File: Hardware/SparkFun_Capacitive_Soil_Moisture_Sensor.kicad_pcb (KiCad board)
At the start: 2 copper layers, 15.2 x 73.4 mm, 53 parts, among them J1 Qwiic_RA, J2 Qwiic_RA, U1 CY8CMBR3102

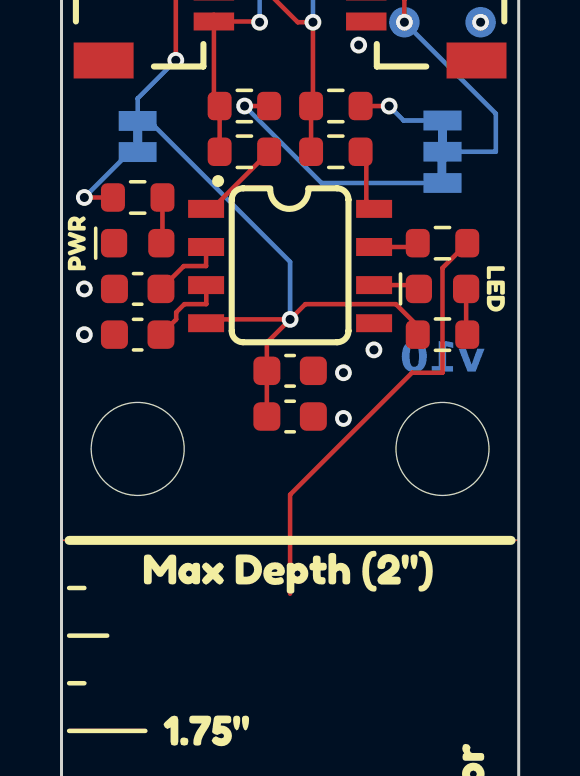
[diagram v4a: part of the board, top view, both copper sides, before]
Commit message: Cleanup symmetry and add measurements
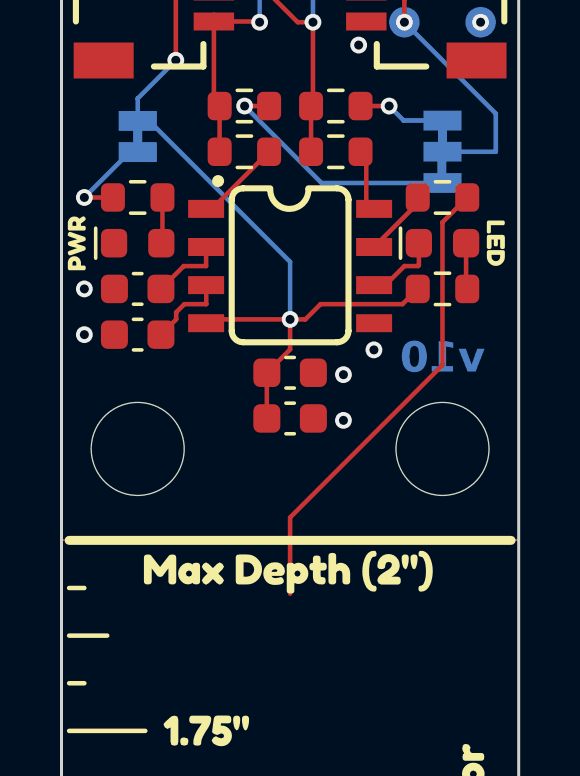
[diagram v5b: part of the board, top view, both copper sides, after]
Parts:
- moved D2 1.52 mm to (120.7, 63.8)
- moved kibuzzard-693C8DE4 1.52 mm to (122.4, 63.8)
- moved R6 1.52 mm to (120.7, 62.2)
- moved R7 1.52 mm to (120.7, 65.3)
- moved C1 0.06 mm to (115.6, 69.6)
- moved C2 0.06 mm to (115.6, 68.1)
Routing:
- net Net-(D2-K): track 1.55 -> 2.50 mm
- net TO_CAP_PLATE: track 14.7 -> 15.7 mm
- net Net-(U1-CS0): track 1.51 -> 2.25 mm
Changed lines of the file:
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@@
 	(footprint "SparkFun-Resistor:R_0603_1608Metric"
 		(layer "F.Cu")
-		(at 120.65 63.754)
+		(at 120.65 62.23)
 		(descr "Resistor SMD 0603 (1608 Metric), square (rectangular) end terminal, IPC_7351 nominal, (Body size source: IPC-SM-782 page 72, https://www.pcb-3d.com/wordpress/wp-content/uploads/ipc-sm-782a_amendment_1_and_2.pdf), generated with kicad-footprint-generator")
 		(tags "SparkFun resistor")
@@
 	(footprint "SparkFun-Capacitor:C_0603_1608Metric"
 		(layer "F.Cu")
-		(at 115.57 68.008)
+		(at 115.57 68.072)
 		(tags "SparkFun capacitor")
 		(property "Reference" "C2"
@@
 	(footprint "SparkFun-Resistor:R_0603_1608Metric"
 		(layer "F.Cu")
-		(at 120.65 66.802)
+		(at 120.65 65.278)
 		(descr "Resistor SMD 0603 (1608 Metric), square (rectangular) end terminal, IPC_7351 nominal, (Body size source: IPC-SM-782 page 72, https://www.pcb-3d.com/wordpress/wp-content/uploads/ipc-sm-782a_amendment_1_and_2.pdf), generated with kicad-footprint-generator")
 		(tags "SparkFun resistor")
@@
 	(footprint "SparkFun-Capacitor:C_0603_1608Metric"
 		(layer "F.Cu")
-		(at 115.57 69.532)
+		(at 115.57 69.596)
 		(tags "SparkFun capacitor")
 		(property "Reference" "C1"
@@
 	(footprint "SparkFun-LED:LED_0603_1608Metric_Red"
 		(layer "F.Cu")
-		(at 120.65 65.278)
+		(at 120.65 63.754)
 		(tags "SparkFun LED")
 		(property "Reference" "D2"
@@
 				(font
 					(size 0.001 0.001)
+					(thickness 0.15)
 				)
 			)
@@
 				(font
 					(size 0.001 0.001)
+					(thickness 0.15)
 				)
 			)
@@
 	(footprint "kibuzzard-693C8DE4"
 		(layer "F.Cu")
-		(at 122.428 65.278 -90)
+		(at 122.428 63.754 -90)
 		(descr "Generated with KiBuzzard")
 		(tags "kb_params=eyJBbGlnbm1lbnRDaG9pY2UiOiAiQ2VudGVyIiwgIkNhcExlZnRDaG9pY2UiOiAiKCIsICJDYXBSaWdodENob2ljZSI6ICJdIiwgIkZvbnRDb21ib0JveCI6ICJGcmVkZHlTcGFyay1SZWd1bGFyIiwgIkhlaWdodEN0cmwiOiAwLjYsICJMYXllckNvbWJvQm94IjogIkYuU2lsa1MiLCAiTGluZVNwYWNpbmdDdHJsIjogMS41LCAiTXVsdGlMaW5lVGV4dCI6ICJMRUQiLCAiUGFkZGluZ0JvdHRvbUN0cmwiOiAzLjAsICJQYWRkaW5nTGVmdEN0cmwiOiAzLjAsICJQYWRkaW5nUmlnaHRDdHJsIjogMy4wLCAiUGFkZGluZ1RvcEN0cmwiOiAzLjAsICJXaWR0aEN0cmwiOiAwLjYsICJhZHZhbmNlZENoZWNrYm94IjogdHJ1ZSwgImlubGluZUZvcm1hdFRleHRib3giOiB0cnVlLCAibGluZW92ZXJTdHlsZUNob2ljZSI6ICJTcXVhcmUiLCAibGluZW92ZXJUaGlja25lc3NDdHJsIjogMX0=")
@@
 				(font
 					(size 0.001 0.001)
+					(thickness 0.15)
 				)
 			)
@@
 				(font
 					(size 0.001 0.001)
+					(thickness 0.15)
 				)
 			)
@@
 		(layer "Dwgs.User")
 		(pts
-			(xy 107.95 49.53) (xy 123.19 51.054)
+			(xy 107.95 50.038) (xy 123.19 51.562)
 		)
-		(height -5.588)
+		(height -2.286)
 		(orientation 0)
 		(format
@@
 		)
 		(gr_text "0.6 in"
-			(at 105.156 43.942 0)
+			(at 105.156 47.752 0)
+			(layer "Dwgs.User")
+			(effects
+				(font
+					(size 1 1)
+					(thickness 0.15)
+				)
+			)
+		)
+	)
+	(dimension
+		(type orthogonal)
+		(layer "Dwgs.User")
+		(pts
+			(xy 107.188 51.054) (xy 109.982 70.612)
+		)
+		(height 22.352)
+		(orientation 1)
+		(format
+			(prefix "")
+			(suffix "")
+			(units 3)
+			(units_format 1)
+			(precision 4)
+			(suppress_zeroes yes)
+		)
+		(style
+			(thickness 0.15)
+			(arrow_length 1.27)
+			(text_position_mode 2)
+			(arrow_direction outward)
+			(extension_height 0.58642)
+			(extension_offset 0.5)
+			(keep_text_aligned yes)
+		)
+		(gr_text "0.77 in"
+			(at 129.54 47.498 90)
+			(layer "Dwgs.User")
+			(effects
+				(font
+					(size 1 1)
+					(thickness 0.15)
+				)
+			)
+		)
+	)
+	(dimension
+		(type orthogonal)
+		(layer "Dwgs.User")
+		(pts
+			(xy 107.95 51.054) (xy 108.458 63.754)
+		)
+		(height 19.558)
+		(orientation 1)
+		(format
+			(prefix "")
+			(suffix "")
+			(units 3)
+			(units_format 1)
+			(precision 4)
+			(suppress_zeroes yes)
+		)
+		(style
+			(thickness 0.15)
+			(arrow_length 1.27)
+			(text_position_mode 2)
+			(arrow_direction outward)
+			(extension_height 0.58642)
+			(extension_offset 0.5)
+			(keep_text_aligned yes)
+		)
+		(gr_text "0.5 in"
+			(at 127.508 48.006 90)
+			(layer "Dwgs.User")
+			(effects
+				(font
+					(size 1 1)
+					(thickness 0.15)
+				)
+			)
+		)
+	)
+	(dimension
+		(type orthogonal)
+		(layer "Dwgs.User")
+		(pts
+			(xy 107.95 71.12) (xy 110.49 71.12)
+		)
+		(height -21.336)
+		(orientation 0)
+		(format
+			(prefix "")
+			(suffix "")
+			(units 3)
+			(units_format 1)
+			(precision 4)
+			(suppress_zeroes yes)
+		)
+		(style
+			(thickness 0.15)
+			(arrow_length 1.27)
+			(text_position_mode 2)
+			(arrow_direction outward)
+			(extension_height 0.58642)
+			(extension_offset 0.5)
+			(keep_text_aligned yes)
+		)
+		(gr_text "0.1 in"
+			(at 105.156 49.53 0)
 			(layer "Dwgs.User")
 			(effects
@@
 	)
 	(segment
+		(start 115.57 66.294)
+		(end 116.078 66.294)
+		(width 0.1524)
+		(layer "F.Cu")
+		(net 1)
+	)
+	(segment
 		(start 116.07 55.364)
 		(end 118.11 55.364)
@@
 	)
 	(segment
-		(start 114.795 69.532)
-		(end 114.795 68.008)
+		(start 114.795 69.596)
+		(end 114.795 68.072)
 		(width 0.1524)
 		(layer "F.Cu")
@@
 	)
 	(segment
-		(start 119.825 66.5168)
-		(end 119.0942 65.786)
+		(start 115.036 67.831)
+		(end 115.57 67.297)
 		(width 0.1524)
 		(layer "F.Cu")
@@
 	)
 	(segment
-		(start 119.0942 65.786)
-		(end 116.078 65.786)
+		(start 116.586 65.786)
+		(end 119.317 65.786)
 		(width 0.1524)
 		(layer "F.Cu")
@@
 	)
 	(segment
-		(start 116.078 65.786)
-		(end 115.57 66.294)
+		(start 119.317 65.786)
+		(end 119.825 65.278)
 		(width 0.1524)
 		(layer "F.Cu")
@@
 	)
 	(segment
-		(start 115.07 54.364)
-		(end 116.07 55.364)
-		(width 0.508)
+		(start 114.795 67.831)
+		(end 115.036 67.831)
+		(width 0.1524)
 		(layer "F.Cu")
 		(net 1)
 	)
 	(segment
-		(start 119.825 66.802)
-		(end 119.825 66.5168)
+		(start 114.795 68.072)
+		(end 114.795 67.895)
 		(width 0.1524)
 		(layer "F.Cu")
@@
 	)
 	(segment
-		(start 114.795 68.008)
-		(end 114.795 67.069)
-		(width 0.1524)
+		(start 115.07 54.364)
+		(end 116.07 55.364)
+		(width 0.508)
 		(layer "F.Cu")
 		(net 1)
@@
 	)
 	(segment
+		(start 116.078 66.294)
+		(end 116.586 65.786)
+		(width 0.1524)
+		(layer "F.Cu")
+		(net 1)
+	)
+	(segment
 		(start 114.808 54.364)
 		(end 115.07 54.364)
@@
 	)
 	(segment
-		(start 114.795 67.069)
-		(end 115.57 66.294)
+		(start 118.11 55.364)
+		(end 119.118 55.364)
 		(width 0.1524)
 		(layer "F.Cu")
@@
 	)
 	(segment
-		(start 118.11 55.364)
-		(end 119.118 55.364)
+		(start 115.57 67.297)
+		(end 115.57 66.294)
 		(width 0.1524)
 		(layer "F.Cu")
@@
 	)
 	(via
-		(at 117.348 68.072)
+		(at 117.348 68.136)
 		(size 0.56)
 		(drill 0.3)
@@
 	)
 	(via
-		(at 117.348 69.596)
+		(at 117.348 69.66)
 		(size 0.56)
 		(drill 0.3)
@@
 	)
 	(segment
-		(start 120.65 68.072)
-		(end 119.634 68.072)
-		(width 0.1524)
-		(layer "F.Cu")
-		(net 11)
-	)
-	(segment
-		(start 115.57 72.136)
-		(end 115.57 75.438)
+		(start 115.57 72.898)
+		(end 120.65 67.818)
 		(width 0.1524)
 		(layer "F.Cu")
@@
 	)
 	(segment
-		(start 119.634 68.072)
-		(end 115.57 72.136)
+		(start 120.65 67.818)
+		(end 120.65 63.055)
 		(width 0.1524)
 		(layer "F.Cu")
@@
 	)
 	(segment
-		(start 120.65 64.579)
-		(end 121.475 63.754)
+		(start 120.65 63.055)
+		(end 121.475 62.23)
 		(width 0.1524)
 		(layer "F.Cu")
@@
 	)
 	(segment
-		(start 120.65 68.072)
-		(end 120.65 64.579)
+		(start 115.57 75.438)
+		(end 115.57 72.898)
 		(width 0.1524)
 		(layer "F.Cu")
@@
 	)
 	(segment
-		(start 119.7355 65.151)
-		(end 119.8625 65.278)
+		(start 118.745 65.151)
+		(end 119.38 64.516)
+		(width 0.1524)
+		(layer "F.Cu")
+		(net 14)
+	)
+	(segment
+		(start 119.837 64.516)
+		(end 119.8625 64.4905)
+		(width 0.1524)
+		(layer "F.Cu")
+		(net 14)
+	)
+	(segment
+		(start 119.8625 64.4905)
+		(end 119.8625 63.754)
 		(width 0.1524)
 		(layer "F.Cu")
@@
 	(segment
 		(start 118.37 65.151)
-		(end 119.7355 65.151)
+		(end 118.745 65.151)
 		(width 0.1524)
 		(layer "F.Cu")
@@
 	)
 	(segment
-		(start 121.4375 65.278)
-		(end 121.4375 66.7645)
+		(start 119.38 64.516)
+		(end 119.837 64.516)
+		(width 0.1524)
+		(layer "F.Cu")
+		(net 14)
+	)
+	(segment
+		(start 121.4375 63.754)
+		(end 121.4375 65.2405)
 		(width 0.1524)
 		(layer "F.Cu")
@@
 	)
 	(segment
-		(start 121.4375 66.7645)
-		(end 121.475 66.802)
+		(start 121.4375 65.2405)
+		(end 121.475 65.278)
 		(width 0.1524)
 		(layer "F.Cu")
@@
 	)
 	(segment
-		(start 118.37 63.881)
-		(end 119.698 63.881)
+		(start 119.825 62.426)
+		(end 119.825 62.23)
 		(width 0.1524)
 		(layer "F.Cu")
@@
 	)
 	(segment
-		(start 119.698 63.881)
-		(end 119.825 63.754)
+		(start 118.37 63.881)
+		(end 119.825 62.426)
 		(width 0.1524)
 		(layer "F.Cu")

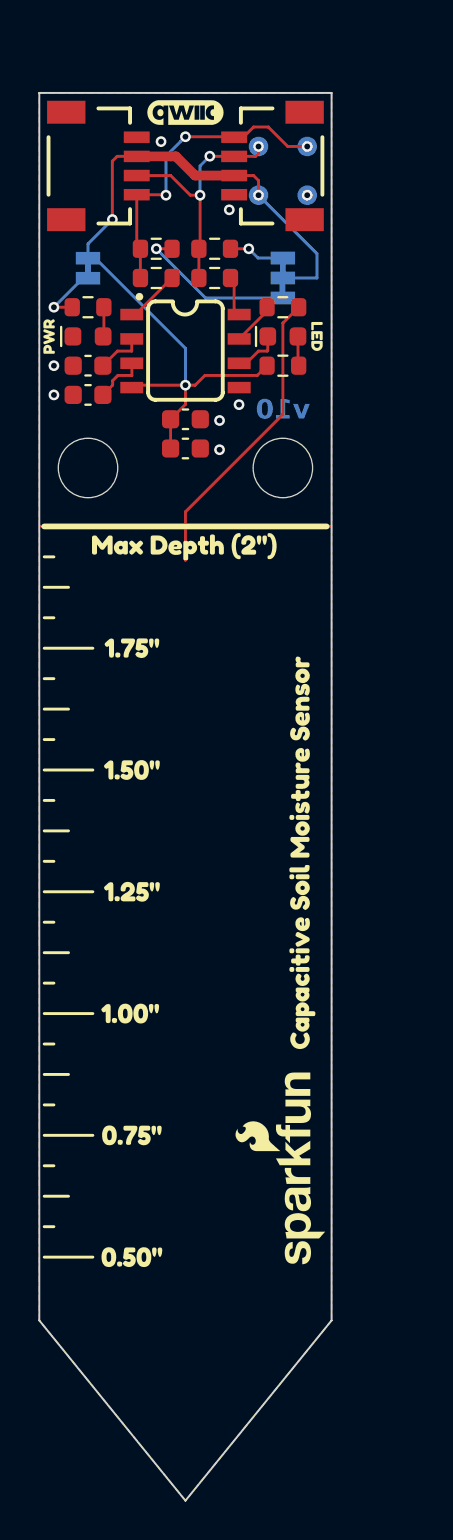
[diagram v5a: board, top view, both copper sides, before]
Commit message: Add PCB fixes from review
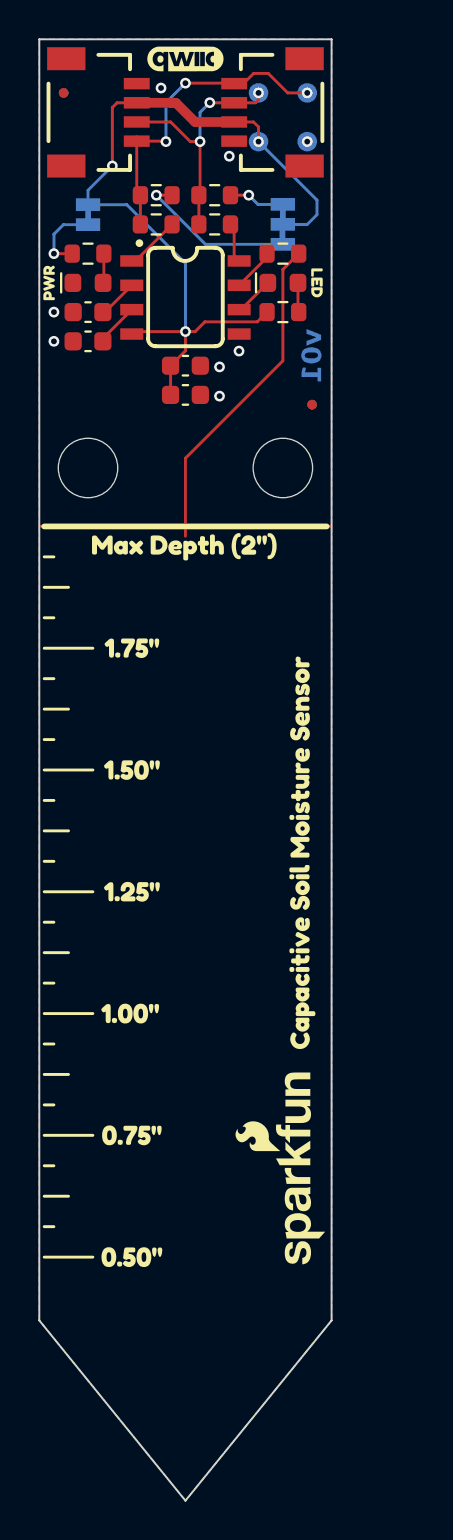
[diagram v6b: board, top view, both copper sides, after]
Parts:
- added FID1: Fiducial_0.5mm, SparkFun-Aesthetic:Fiducial_0.5mm_Mask1mm, B.Cu at (122.2, 67.3)
- added FID2: Fiducial_0.5mm, SparkFun-Aesthetic:Fiducial_0.5mm_Mask1mm, B.Cu at (109.2, 51.1)
- added FID3: Fiducial_0.5mm, SparkFun-Aesthetic:Fiducial_0.5mm_Mask1mm, F.Cu at (109.2, 51.1)
- added FID4: Fiducial_0.5mm, SparkFun-Aesthetic:Fiducial_0.5mm_Mask1mm, F.Cu at (122.2, 67.3)
- D2: value Red -> Blue; footprint SparkFun-LED:LED_0603_1608Metric_Red -> SparkFun-LED:LED_0603_1608Metric_Blue
- R7: value 4.7k -> 2.2k
- moved kibuzzard-693350BE 3.30 mm to (118.4, 57.4)
- moved Ref** 2.97 mm to (111.3, 51.8)
- moved kibuzzard-69334C1A 2.80 mm to (113.2, 57.4)
- moved C4 2.79 mm to (110.5, 64.0)
- moved C3 2.79 mm to (110.5, 62.5)
- moved JP2 2.79 mm to (120.7, 57.9)
- moved R2 2.79 mm to (114.0, 56.4)
- moved R3 2.79 mm to (117.1, 56.4)
- moved R4 2.79 mm to (117.1, 57.9)
- moved R5 2.79 mm to (114.0, 57.9)
- moved R7 2.79 mm to (120.7, 62.5)
- moved U1 2.79 mm to (115.6, 61.7)
- moved kibuzzard-69371667 2.79 mm to (119.4, 50.0)
- moved kibuzzard-6937166E 2.79 mm to (121.9, 50.0)
- moved C1 2.79 mm to (115.6, 66.8)
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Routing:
- net TO_CAP_PLATE: track 15.7 -> 17.2 mm
- net 3.3V: track 42.1 -> 42.8 mm
- net Net-(JP1-A): track 3.36 -> 3.95 mm
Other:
- board size 15.2 x 73.4 mm -> 15.2 x 76.2 mm
- board text added: "Finish: Finish: ENIG"
- board text added: "Route Out"
- board text added: "v01"
- board text removed: "Finish: Lead-Free HASL"
- board text removed: "v10"

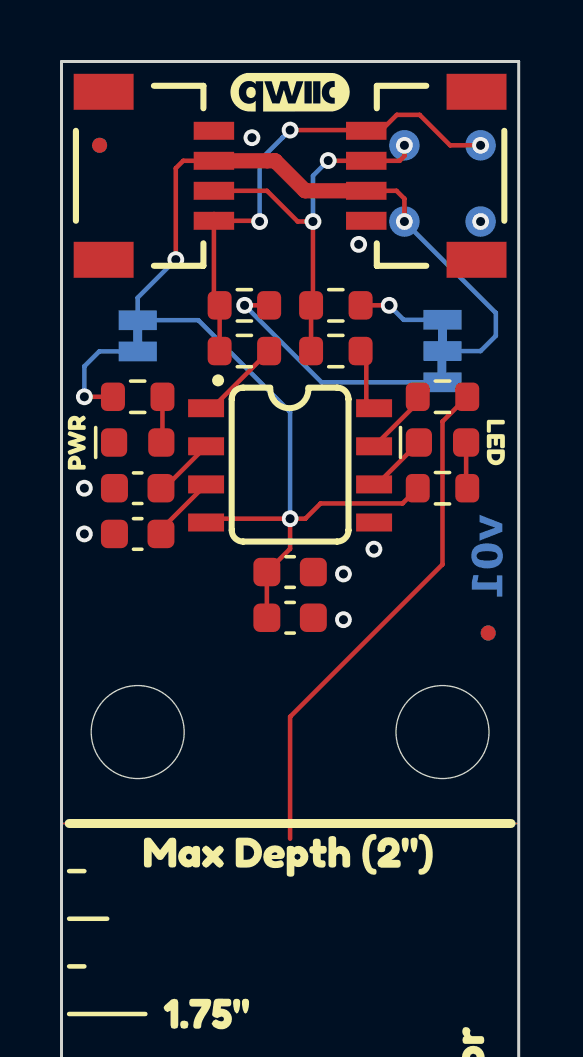
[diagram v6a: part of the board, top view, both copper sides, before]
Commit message: Create version of the PCB with components alligned to 12.5mil grid
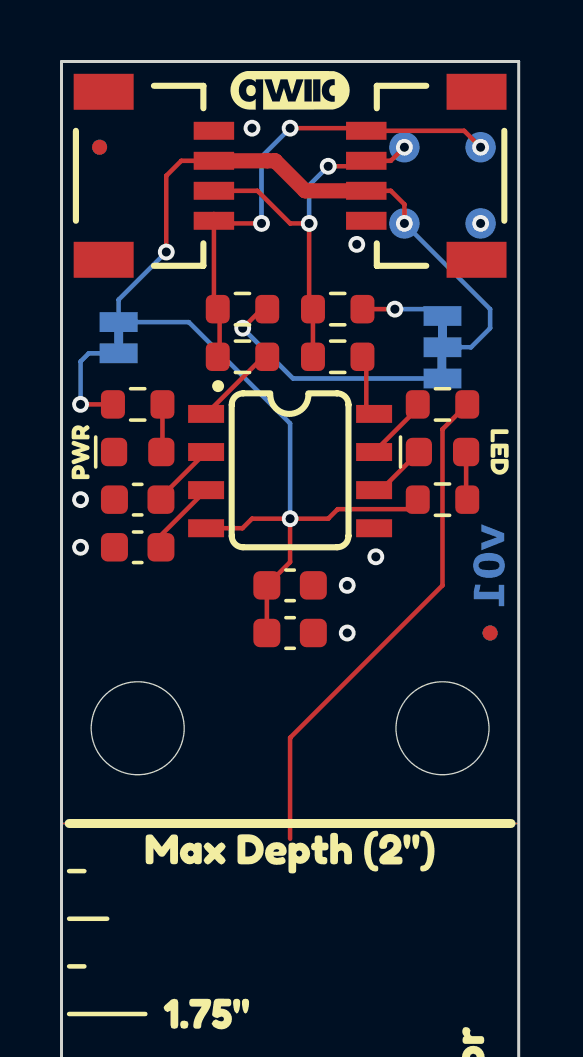
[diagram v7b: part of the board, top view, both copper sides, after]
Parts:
- moved kibuzzard-69334C1A 0.65 mm to (112.5, 57.5)
- moved JP1 0.64 mm to (109.9, 57.5)
- moved C1 0.51 mm to (115.6, 67.3)
- moved C4 0.44 mm to (110.5, 64.5)
- moved C2 0.44 mm to (115.6, 65.7)
- moved C3 0.38 mm to (110.5, 62.9)
- moved R7 0.38 mm to (120.7, 62.9)
- moved kibuzzard-693C8DE4 0.34 mm to (122.6, 61.3)
- moved kibuzzard-693C8DDA 0.34 mm to (108.6, 61.3)
- moved D1 0.32 mm to (110.5, 61.3)
- moved D2 0.32 mm to (120.7, 61.3)
- moved R1 0.25 mm to (110.5, 59.7)
- moved R6 0.25 mm to (120.7, 59.7)
- moved R4 0.20 mm to (117.2, 58.1)
- moved R5 0.20 mm to (114.0, 58.1)
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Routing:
- net 3.3V: track 42.8 -> 43.5 mm
